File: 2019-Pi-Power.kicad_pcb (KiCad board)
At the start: 2 copper layers, 65 x 56 mm, 128 parts, among them J1 Barrel_Jack_Switch, J2 USB_A, J3 USB_A, J4 Conn_02x04_Odd_Even, J5 Conn_01x04, J6 Conn_01x04, J7 Conn_01x04, J8 Conn_02x02_Odd_Even, P1 Conn_02x20_Odd_Even, U1 MP1584

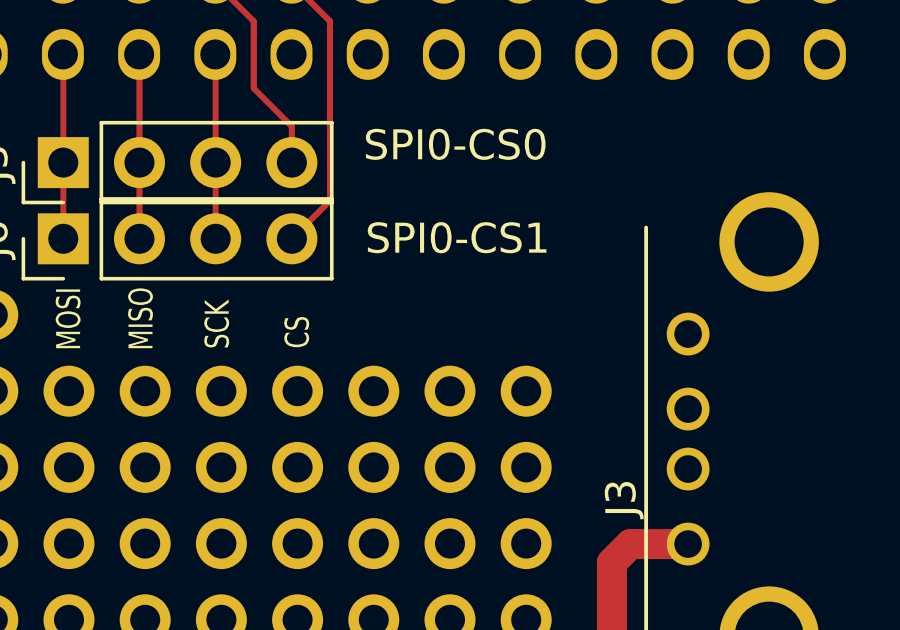
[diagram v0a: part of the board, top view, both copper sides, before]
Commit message: Update component Values
Add BOM
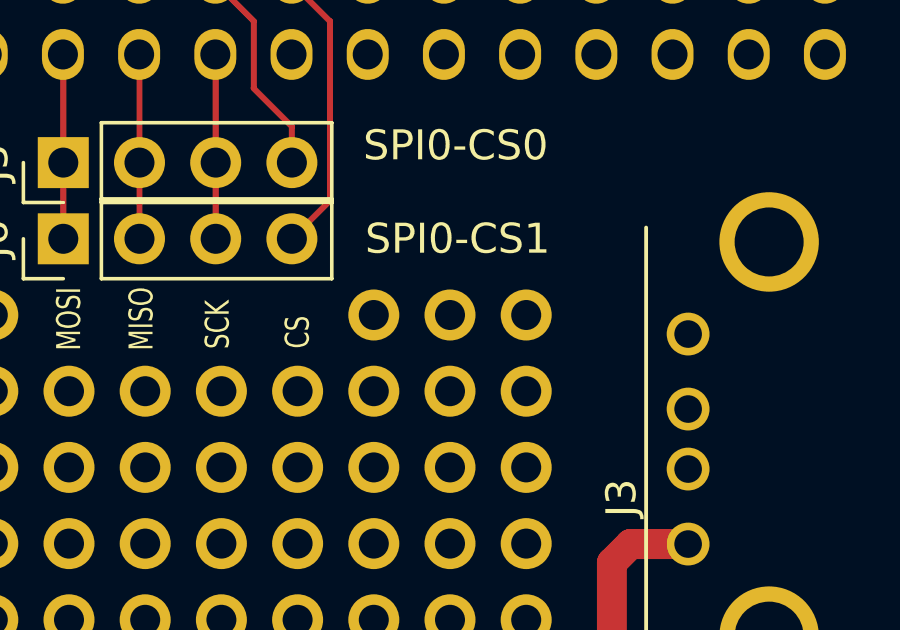
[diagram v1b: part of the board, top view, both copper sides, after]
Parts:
- added 0: SolderWirePad_single_0-8mmDrill, Wire_Pads:SolderWirePad_single_0-8mmDrill, F.Cu at (246.7, 107.5)
- added 0: SolderWirePad_single_0-8mmDrill, Wire_Pads:SolderWirePad_single_0-8mmDrill, F.Cu at (244.1, 107.5)
- added 0: SolderWirePad_single_0-8mmDrill, Wire_Pads:SolderWirePad_single_0-8mmDrill, F.Cu at (241.6, 107.5)
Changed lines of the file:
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@@
     (tracks 113)
     (zones 0)
-    (modules 128)
+    (modules 131)
     (nets 45)
   )
@@
   )
   (module Wire_Pads:SolderWirePad_single_0-8mmDrill (layer F.Cu)
+    (at 246.6725 107.455)
+    (fp_text reference 0 (at 0.254 0.127) (layer F.SilkS) hide
+      (effects (font (size 1 1) (thickness 0.15)))
+    )
+    (fp_text value SolderWirePad_single_0-8mmDrill (at 0 2.54) (layer F.Fab)
+      (effects (font (size 1 1) (thickness 0.15)))
+    )
+    (pad 1 thru_hole oval (at 0 0) (size 1.7 1.7) (drill 1) (layers *.Cu *.Mask))
+  )
+  (module Wire_Pads:SolderWirePad_single_0-8mmDrill (layer F.Cu)
+    (at 244.1325 107.455)
+    (fp_text reference 0 (at 0.254 0.127) (layer F.SilkS) hide
+      (effects (font (size 1 1) (thickness 0.15)))
+    )
+    (fp_text value SolderWirePad_single_0-8mmDrill (at 0 2.54) (layer F.Fab)
+      (effects (font (size 1 1) (thickness 0.15)))
+    )
+    (pad 1 thru_hole oval (at 0 0) (size 1.7 1.7) (drill 1) (layers *.Cu *.Mask))
+  )
+  (module Wire_Pads:SolderWirePad_single_0-8mmDrill (layer F.Cu)
+    (at 241.5925 107.455)
+    (fp_text reference 0 (at 0.254 0.127) (layer F.SilkS) hide
+      (effects (font (size 1 1) (thickness 0.15)))
+    )
+    (fp_text value SolderWirePad_single_0-8mmDrill (at 0 2.54) (layer F.Fab)
+      (effects (font (size 1 1) (thickness 0.15)))
+    )
+    (pad 1 thru_hole oval (at 0 0) (size 1.7 1.7) (drill 1) (layers *.Cu *.Mask))
+  )
+  (module Wire_Pads:SolderWirePad_single_0-8mmDrill (layer F.Cu)
     (at 239.0525 130.315)
     (fp_text reference 0 (at 0.381 0.127) (layer F.SilkS) hide
@@
     (pad 1 thru_hole rect (at 0 0 90) (size 3.5 3.5) (drill oval 1 3) (layers *.Cu *.Mask)
       (net 30 "Net-(C1-Pad1)"))
+    (model D:/KiCad/library/steps/CUI_PJ-002A.step
+      (offset (xyz -13.7 0 6.5))
+      (scale (xyz 1 1 1))
+      (rotate (xyz -90 0 180))
+    )
   )
   (module Inductors_SMD:L_10.4x10.4_H4.8 (layer F.Cu)
@@
     (pad 1 thru_hole rect (at 0 0 90) (size 1.7 1.7) (drill 1) (layers *.Cu *.Mask)
       (net 3 GND))
-    (model ${KISYS3DMOD}/Pin_Headers.3dshapes/Pin_Header_Straight_2x04_Pitch2.54mm.wrl
-      (at (xyz 0 0 0))
-      (scale (xyz 1 1 1))
-      (rotate (xyz 0 0 0))
-    )
   )
   (module Pin_Headers:Pin_Header_Straight_1x04_Pitch2.54mm (layer F.Cu)
@@
     (pad 4 thru_hole oval (at 0 7.62 90) (size 1.7 1.7) (drill 1) (layers *.Cu *.Mask)
       (net 43 /SPI0_CE_0))
-    (model ${KISYS3DMOD}/Pin_Headers.3dshapes/Pin_Header_Straight_1x04_Pitch2.54mm.wrl
-      (at (xyz 0 0 0))
-      (scale (xyz 1 1 1))
-      (rotate (xyz 0 0 0))
-    )
   )
   (module Pin_Headers:Pin_Header_Straight_1x04_Pitch2.54mm (layer F.Cu)
@@
     (pad 1 thru_hole rect (at 0 0 90) (size 1.7 1.7) (drill 1) (layers *.Cu *.Mask)
       (net 21 "/GPIO10(SPI0_MOSI)"))
-    (model ${KISYS3DMOD}/Pin_Headers.3dshapes/Pin_Header_Straight_1x04_Pitch2.54mm.wrl
-      (at (xyz 0 0 0))
-      (scale (xyz 1 1 1))
-      (rotate (xyz 0 0 0))
-    )
   )
   (module Symbols:Symbol_Barrel_Polarity (layer F.Cu)
@@
     (pad 1 thru_hole rect (at 0 0 90) (size 1.7 1.7) (drill 1) (layers *.Cu *.Mask)
       (net 2 +5V))
-    (model ${KISYS3DMOD}/Pin_Headers.3dshapes/Pin_Header_Straight_1x04_Pitch2.54mm.wrl
-      (at (xyz 0 0 0))
-      (scale (xyz 1 1 1))
-      (rotate (xyz 0 0 0))
-    )
   )
   (module Pin_Headers:Pin_Header_Straight_2x02_Pitch2.54mm (layer F.Cu)
@@
     (pad 1 thru_hole rect (at 0 0 90) (size 1.7 1.7) (drill 1) (layers *.Cu *.Mask)
       (net 3 GND))
-    (model ${KISYS3DMOD}/Pin_Headers.3dshapes/Pin_Header_Straight_2x02_Pitch2.54mm.wrl
-      (at (xyz 0 0 0))
-      (scale (xyz 1 1 1))
-      (rotate (xyz 0 0 0))
-    )
-  )
-  (module Wire_Pads:SolderWirePad_single_0-8mmDrill (layer F.Cu)
+  )
+  (module Wire_Pads:SolderWirePad_single_0-8mmDrill (layer F.Cu)

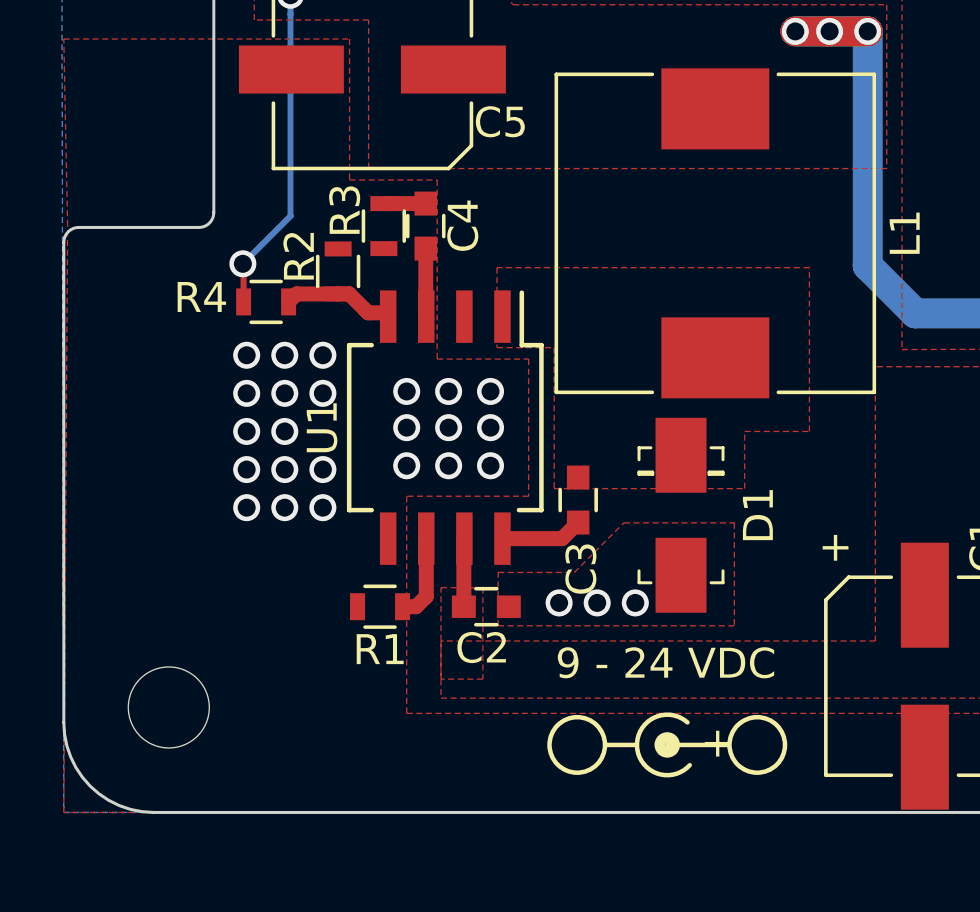
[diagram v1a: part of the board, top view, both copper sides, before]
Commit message: Fix footprint MP1584
Was too wide, grabbed the wrong one.

Also added thermal reliefs.
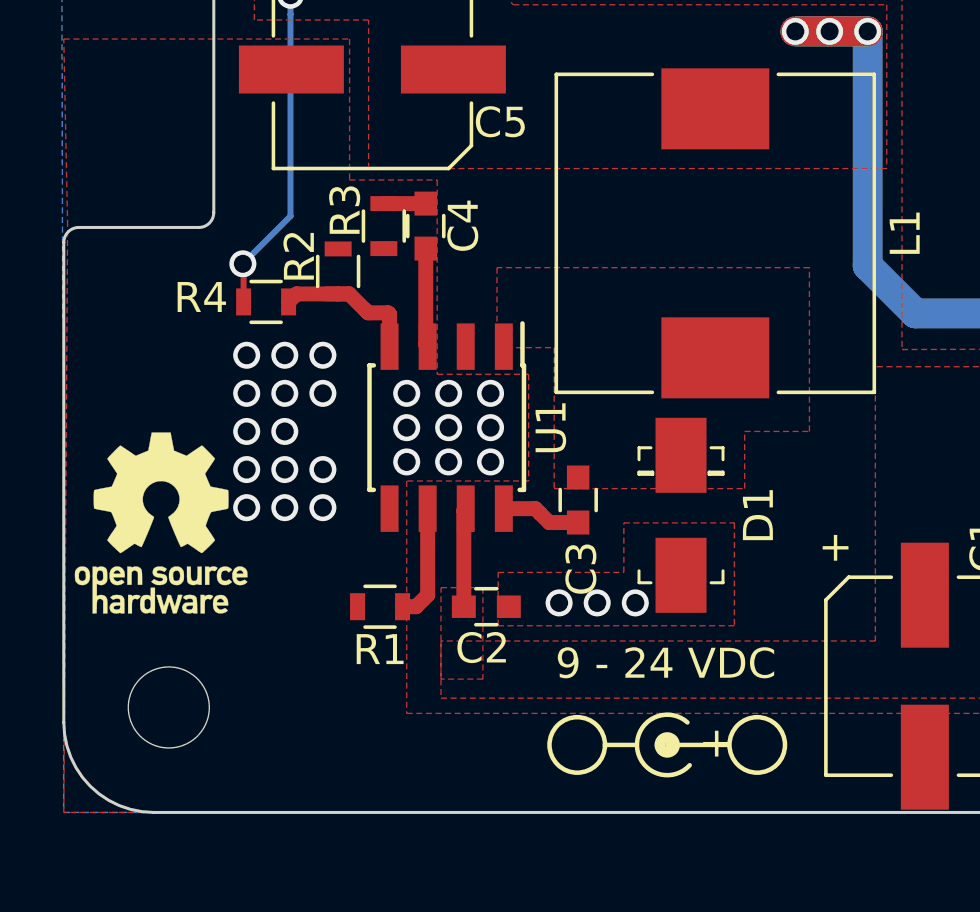
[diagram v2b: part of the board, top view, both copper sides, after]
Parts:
- added REF***: OSHW-Logo_5.7x6mm_SilkScreen, Symbols:OSHW-Logo_5.7x6mm_SilkScreen, F.Cu at (203.2, 140.3)
- U1: footprint Housings_SOIC:SO-8_5.3x6.2mm_Pitch1.27mm -> Housings_SOIC:SOIC-8_3.9x4.9mm_Pitch1.27mm
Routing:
- net Net-(C4-Pad1): track 2.15 -> 3.30 mm
- net Net-(R2-Pad1): track 3.69 -> 4.84 mm
- net Net-(R1-Pad1): track 2.86 -> 3.88 mm
- net Net-(C1-Pad1): track 2.28 -> 3.30 mm
